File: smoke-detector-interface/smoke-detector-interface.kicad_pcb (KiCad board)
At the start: 2 copper layers, 55.9 x 106.7 mm, 28 parts, among them J1 Conn_01x04_Pin, J2 M50-3500542, J3 DE9_Receptacle, J4 61200621621, J5 Conn_01x06_Pin, U1 UA78L10ACLPRE3, U2 AS7805AT, U3 ATtiny13A-P

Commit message: WIP
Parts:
- JP1: footprint TestPoint:TestPoint_Bridge_Pitch2.54mm_Drill0.7mm -> Resistor_THT:R_Axial_DIN0204_L3.6mm_D1.6mm_P7.62mm_Horizontal
- moved JP1 16.2 mm to (149.9, 127.6), turned to -90 degrees
- moved R3 10.8 mm to (121.3, 112.4)
- moved C4 9.71 mm to (135.8, 109.9)
- moved C9 7.54 mm to (143.5, 137.2), turned to 180 degrees
- moved C3 5.85 mm to (125.8, 109.9)
- moved C2 1.33 mm to (143.2, 142.2)
- moved C1 0.90 mm to (148.0, 118.8)
- moved U3 0.90 mm to (136.5, 118.8)
- moved D2 0.64 mm to (129.5, 116.2)
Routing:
- net +5V: track 43.3 -> 129.7 mm
- net +12V: track 71.3 -> 107.1 mm
- net HOSTTX: track 44.0 -> 70.7 mm
- net HOSTRX: track 94.7 -> 73.0 mm
- net Net-(J5-Pin_4): track 0.00 -> 17.3 mm
- net Net-(J2-Pad9): track 33.2 -> 23.3 mm
- net Net-(U3-PB2): track 10.9 -> 15.1 mm
- net Net-(D2-K): track 11.4 -> 15.3 mm
- net Net-(U3-PB1): track 18.9 -> 21.4 mm
- net Net-(U3-PB0): track 22.2 -> 20.3 mm
- net +10V: track 18.1 -> 17.0 mm
- added copper zone on B.Cu, net GND
- removed copper zone on B.Cu, net +12V

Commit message: Improved routing.
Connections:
- net Net-(U3-PB0) renamed MOSI
- net Net-(U3-PB1) renamed MISO
- net Net-(U3-PB2) renamed SCK
- J4 pad 5: Net-(U3-~{RESET}/PB5) -> _RESET
- J5 pad 3: HOSTTX -> Net-(J5-Pin_3)
- J5 pad 4: Net-(J5-Pin_4) -> HOSTRX
- JP1 pad 1: HOSTRX -> HOSTTX
- JP1 pad 2: Net-(J5-Pin_4) -> Net-(J5-Pin_3)
- U3 pad 1: Net-(U3-~{RESET}/PB5) -> _RESET
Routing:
- net _RESET: track 0.00 -> 59.6 mm
- net HOSTRX: track 73.0 -> 91.6 mm
- net Net-(J5-Pin_4): track 17.3 -> 0.00 mm
- net Net-(U3-~{RESET}/PB5): track 13.0 -> 0.00 mm
- net +5V: track 129.7 -> 135.8 mm
- net MISO: track 21.4 -> 23.2 mm
- net MOSI: track 20.3 -> 21.9 mm

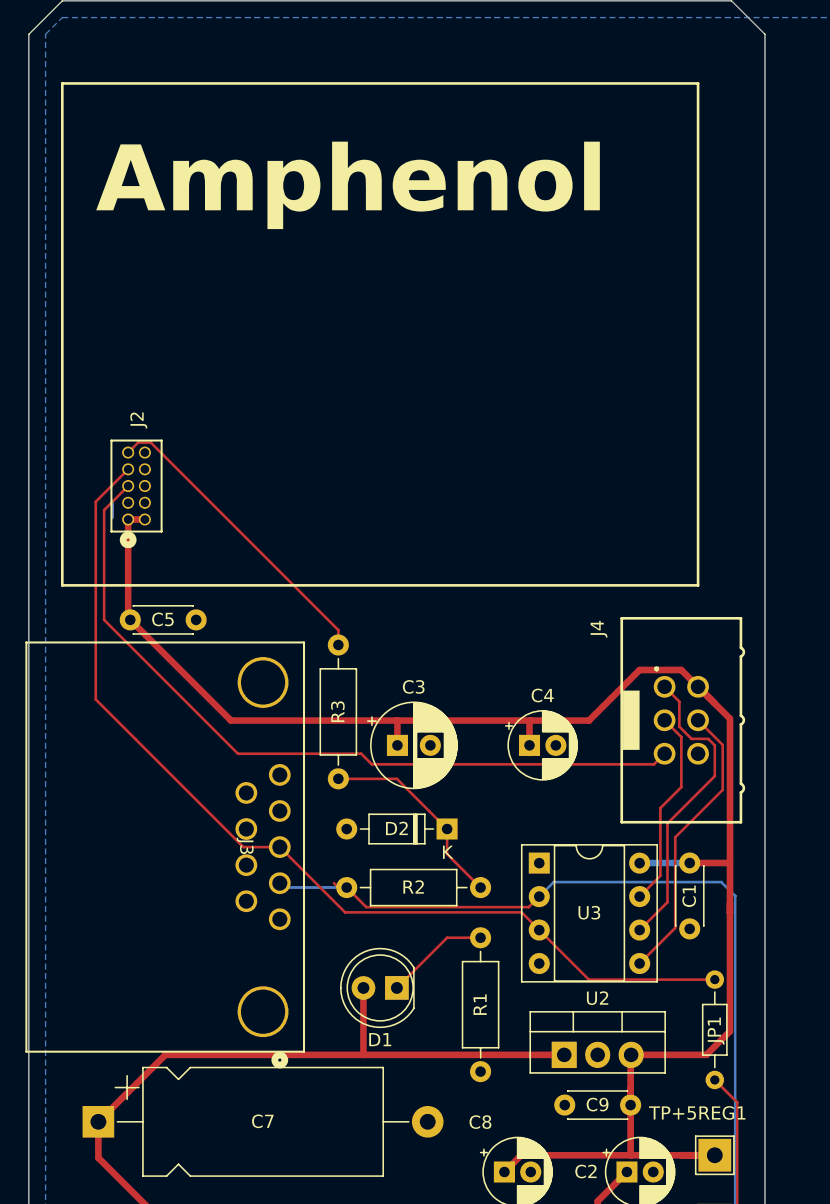
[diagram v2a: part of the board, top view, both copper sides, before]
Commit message: Updates for Zenerglass parts.
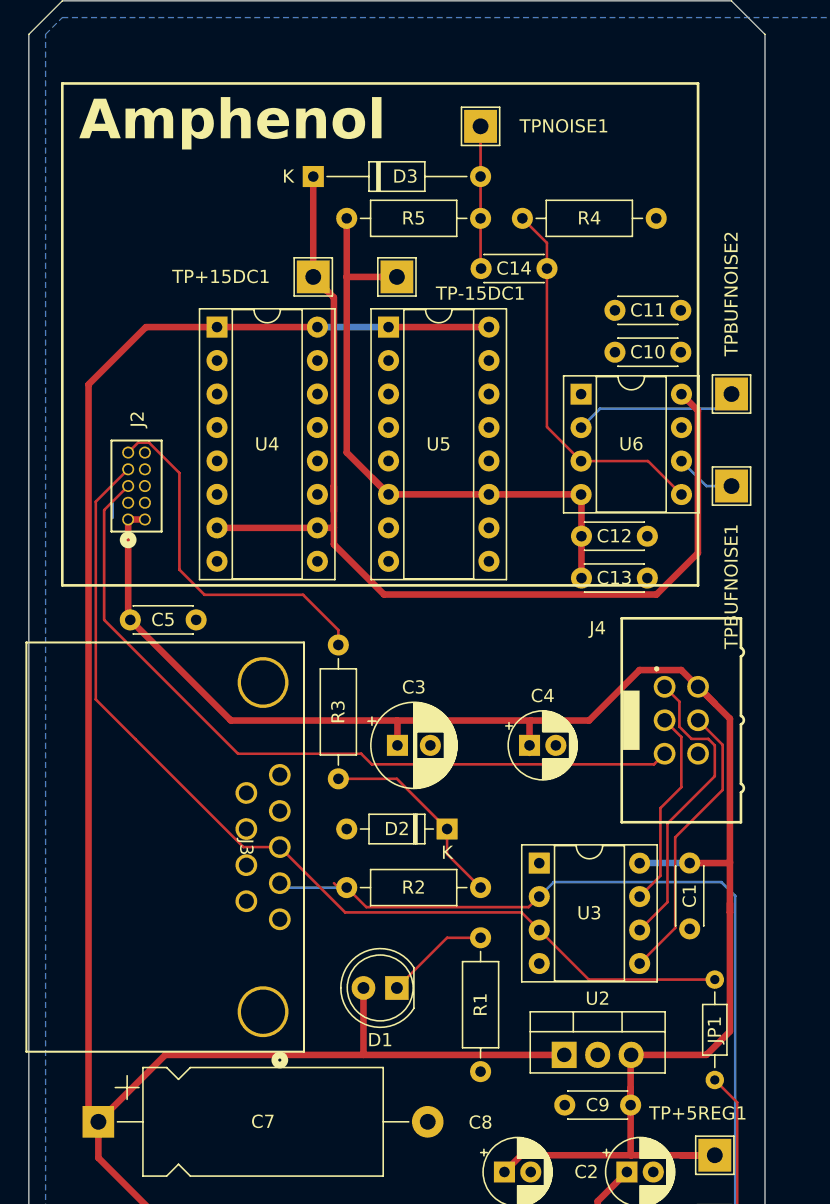
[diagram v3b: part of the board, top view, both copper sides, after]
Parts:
- added C10: 100n, Capacitor_THT:C_Disc_D4.3mm_W1.9mm_P5.00mm, F.Cu at (147.3, 80.0)
- added C11: 1u, Capacitor_THT:C_Disc_D4.3mm_W1.9mm_P5.00mm, F.Cu at (147.3, 76.8)
- added C12: 1u, Capacitor_THT:C_Disc_D4.3mm_W1.9mm_P5.00mm, F.Cu at (139.7, 94.0)
- added C13: 100n, Capacitor_THT:C_Disc_D4.3mm_W1.9mm_P5.00mm, F.Cu at (139.7, 97.2)
- added C14: 1u FILM, Capacitor_THT:C_Disc_D4.3mm_W1.9mm_P5.00mm, F.Cu at (132.1, 73.7)
- added D3: BZX79-C24, Diode_THT:D_DO-35_SOD27_P12.70mm_Horizontal, F.Cu at (119.4, 66.7)
- added R4: 1meg, Resistor_THT:R_Axial_DIN0207_L6.3mm_D2.5mm_P10.16mm_Horizontal, F.Cu at (135.3, 69.8)
- added R5: 100k, Resistor_THT:R_Axial_DIN0207_L6.3mm_D2.5mm_P10.16mm_Horizontal, F.Cu at (132.1, 69.8)
- added TP+15DC1: +15, TestPoint:TestPoint_THTPad_2.5x2.5mm_Drill1.2mm, F.Cu at (119.4, 74.3)
- added TP-15DC1: -15, TestPoint:TestPoint_THTPad_2.5x2.5mm_Drill1.2mm, F.Cu at (125.7, 74.3)
- added TPBUFNOISE1: BUFNOISE, TestPoint:TestPoint_THTPad_2.5x2.5mm_Drill1.2mm, F.Cu at (151.1, 90.2)
- added TPBUFNOISE2: BUFNOISE, TestPoint:TestPoint_THTPad_2.5x2.5mm_Drill1.2mm, F.Cu at (151.1, 83.2)
- added TPNOISE1: NOISE, TestPoint:TestPoint_THTPad_2.5x2.5mm_Drill1.2mm, F.Cu at (132.1, 62.9)
- added U4: ~, Package_DIP:DIP-16_W7.62mm_Socket, F.Cu at (112.1, 78.1)
- added U5: ~, Package_DIP:DIP-16_W7.62mm_Socket, F.Cu at (125.1, 78.1)
- added U6: TL072, Package_DIP:DIP-8_W7.62mm_Socket, F.Cu at (139.7, 83.2)
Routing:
- net +12V: track 107.1 -> 195.6 mm
- net +15V: track 0.00 -> 82.5 mm
- net -15V: track 0.00 -> 48.8 mm
- net Net-(U6A-+): track 0.00 -> 28.9 mm
- net Net-(U6A--): track 0.00 -> 12.5 mm
- net Net-(D3-A): track 0.00 -> 10.8 mm
- net Net-(U6B--): track 0.00 -> 4.58 mm
- net Net-(J2-Pad9): track 23.3 -> 27.6 mm

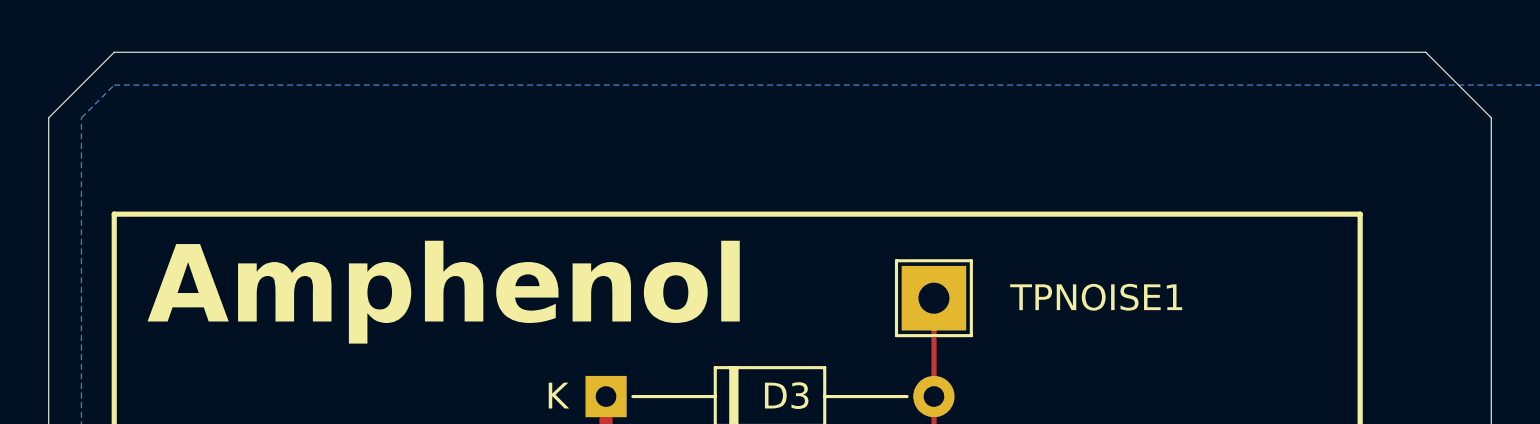
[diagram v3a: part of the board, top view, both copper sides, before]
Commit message: Add mounting holes.
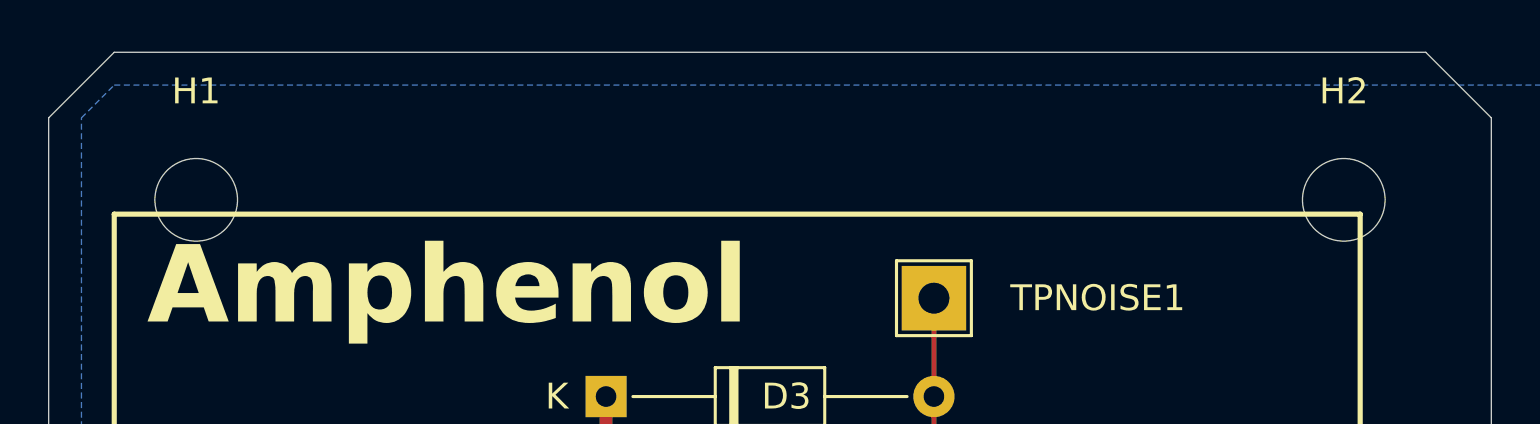
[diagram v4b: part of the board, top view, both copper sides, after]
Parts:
- added H1: MountingHole, MountingHole:MountingHole_3.2mm_M3, F.Cu at (103.5, 59.1)
- added H2: MountingHole, MountingHole:MountingHole_3.2mm_M3, F.Cu at (148.0, 59.1)
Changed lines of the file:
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@@
 		(tags "C Disc series Radial pin pitch 5.00mm  diameter 4.3mm width 1.9mm Capacitor")
 		(property "Reference" "C14"
-			(at 2.5 0 360)
+			(at 2.5 0 0)
 			(layer "F.SilkS")
 			(effects
@@
 		)
 		(property "Value" "1u FILM"
-			(at 2.5 2.2 360)
+			(at 2.5 2.2 0)
 			(layer "F.Fab")
 			(effects
@@
 		)
 		(fp_text user "${REFERENCE}"
-			(at 2.5 0 360)
+			(at 2.5 0 0)
 			(layer "F.Fab")
 			(effects
@@
 		(tags "Resistor Axial_DIN0207 series Axial Horizontal pin pitch 10.16mm 0.25W = 1/4W length 6.3mm diameter 2.5mm")
 		(property "Reference" "R5"
-			(at 5.08 0 360)
+			(at 5.08 0 0)
 			(layer "F.SilkS")
 			(effects
@@
 		)
 		(property "Value" "100k"
-			(at 5.08 2.37 360)
+			(at 5.08 2.37 0)
 			(layer "F.Fab")
 			(effects
@@
 		)
 		(fp_text user "${REFERENCE}"
-			(at 5.08 0 360)
+			(at 5.08 0 0)
 			(layer "F.Fab")
 			(effects
@@
 		)
 	)
+	(footprint "MountingHole:MountingHole_3.2mm_M3"
+		(layer "F.Cu")
+		(at 147.955 59.055)
+		(descr "Mounting Hole 3.2mm, no annular, M3")
+		(tags "mounting hole 3.2mm no annular m3")
+		(property "Reference" "H2"
+			(at 0 -4.2 0)
+			(layer "F.SilkS")
+			(effects
+				(font
+					(size 1 1)
+					(thickness 0.15)
+				)
+			)
+		)
+		(property "Value" "MountingHole"
+			(at 0 4.2 0)
+			(layer "F.Fab")
+			(effects
+				(font
+					(size 1 1)
+					(thickness 0.15)
+				)
+			)
+		)
+		(property "Footprint" "MountingHole:MountingHole_3.2mm_M3"
+			(at 0 0 0)
+			(unlocked yes)
+			(layer "F.Fab")
+			(hide yes)
+			(effects
+				(font
+					(size 1.27 1.27)
+					(thickness 0.15)
+				)
+			)
+		)
+		(property "Datasheet" ""
+			(at 0 0 0)
+			(unlocked yes)
+			(layer "F.Fab")
+			(hide yes)
+			(effects
+				(font
+					(size 1.27 1.27)
+					(thickness 0.15)
+				)
+			)
+		)
+		(property "Description" "Mounting Hole without connection"
+			(at 0 0 0)
+			(unlocked yes)
+			(layer "F.Fab")
+			(hide yes)
+			(effects
+				(font
+					(size 1.27 1.27)
+					(thickness 0.15)
+				)
+			)
+		)
+		(property ki_fp_filters "MountingHole*")
+		(sheetname "Root")
+		(sheetfile "smoke-detector-interface.kicad_sch")
+		(attr exclude_from_pos_files exclude_from_bom)
+		(fp_circle
+			(center 0 0)
+			(end 3.2 0)
+			(stroke
+				(width 0.15)
+				(type solid)
+			)
+			(fill none)
+			(layer "Cmts.User")
+		)
+		(fp_circle
+			(center 0 0)
+			(end 3.45 0)
+			(stroke
+				(width 0.05)
+				(type solid)
+			)
+			(fill none)
+			(layer "F.CrtYd")
+		)
+		(fp_text user "${REFERENCE}"
+			(at 0 0 0)
+			(layer "F.Fab")
+			(effects
+				(font
+					(size 1 1)
+					(thickness 0.15)
+				)
+			)
+		)
+		(pad "" np_thru_hole circle
+			(at 0 0)
+			(size 3.2 3.2)
+			(drill 3.2)
+			(layers "*.Cu" "*.Mask")
+		)
+	)
 	(footprint "Package_TO_SOT_THT:TO-220-3_Vertical"
 		(layer "F.Cu")
@@
 		)
 	)
+	(footprint "MountingHole:MountingHole_3.2mm_M3"
+		(layer "F.Cu")
+		(at 103.505 59.055)
+		(descr "Mounting Hole 3.2mm, no annular, M3")
+		(tags "mounting hole 3.2mm no annular m3")
+		(property "Reference" "H1"
+			(at 0 -4.2 0)
+			(layer "F.SilkS")
+			(effects
+				(font
+					(size 1 1)
+					(thickness 0.15)
+				)
+			)
+		)
+		(property "Value" "MountingHole"
+			(at 0 4.2 0)
+			(layer "F.Fab")
+			(effects
+				(font
+					(size 1 1)
+					(thickness 0.15)
+				)
+			)
+		)
+		(property "Footprint" "MountingHole:MountingHole_3.2mm_M3"
+			(at 0 0 0)
+			(unlocked yes)
+			(layer "F.Fab")
+			(hide yes)
+			(effects
+				(font
+					(size 1.27 1.27)
+					(thickness 0.15)
+				)
+			)
+		)
+		(property "Datasheet" ""
+			(at 0 0 0)
+			(unlocked yes)
+			(layer "F.Fab")
+			(hide yes)
+			(effects
+				(font
+					(size 1.27 1.27)
+					(thickness 0.15)
+				)
+			)
+		)
+		(property "Description" "Mounting Hole without connection"
+			(at 0 0 0)
+			(unlocked yes)
+			(layer "F.Fab")
+			(hide yes)
+			(effects
+				(font
+					(size 1.27 1.27)
+					(thickness 0.15)
+				)
+			)
+		)
+		(property ki_fp_filters "MountingHole*")
+		(sheetname "Root")
+		(sheetfile "smoke-detector-interface.kicad_sch")
+		(attr exclude_from_pos_files exclude_from_bom)
+		(fp_circle
+			(center 0 0)
+			(end 3.2 0)
+			(stroke
+				(width 0.15)
+				(type solid)
+			)
+			(fill none)
+			(layer "Cmts.User")
+		)
+		(fp_circle
+			(center 0 0)
+			(end 3.45 0)
+			(stroke
+				(width 0.05)
+				(type solid)
+			)
+			(fill none)
+			(layer "F.CrtYd")
+		)
+		(fp_text user "${REFERENCE}"
+			(at 0 0 0)
+			(layer "F.Fab")
+			(effects
+				(font
+					(size 1 1)
+					(thickness 0.15)
+				)
+			)
+		)
+		(pad "" np_thru_hole circle
+			(at 0 0)
+			(size 3.2 3.2)
+			(drill 3.2)
+			(layers "*.Cu" "*.Mask")
+		)
+	)
 	(footprint "Capacitor_THT:CP_Radial_D5.0mm_P2.00mm"
 		(layer "F.Cu")
@@
 		(tags "C Disc series Radial pin pitch 5.00mm  diameter 4.3mm width 1.9mm Capacitor")
 		(property "Reference" "C10"
-			(at 2.5 0 360)
+			(at 2.5 0 0)
 			(layer "F.SilkS")
 			(effects
@@
 		)
 		(property "Value" "100n"
-			(at 2.5 2.2 360)
+			(at 2.5 2.2 0)
 			(layer "F.Fab")
 			(effects
@@
 		)
 		(fp_text user "${REFERENCE}"
-			(at 2.5 0 360)
+			(at 2.5 0 0)
 			(layer "F.Fab")
 			(effects
@@
 		(tags "Diode DO-35_SOD27 series Axial Horizontal pin pitch 12.7mm  length 4mm diameter 2mm")
 		(property "Reference" "D3"
-			(at 6.985 0 360)
+			(at 6.985 0 0)
 			(layer "F.SilkS")
 			(effects
@@
 		)
 		(property "Value" "BZX79-C24"
-			(at 6.35 2.12 360)
+			(at 6.35 2.12 0)
 			(layer "F.Fab")
 			(effects
@@
 		)
 		(fp_text user "K"
-			(at -1.905 0 360)
+			(at -1.905 0 0)
 			(layer "F.SilkS")
 			(effects
@@
 		)
 		(fp_text user "K"
-			(at 0 -1.8 360)
+			(at 0 -1.8 0)
 			(layer "F.Fab")
 			(effects
@@
 		)
 		(fp_text user "${REFERENCE}"
-			(at 6.65 0 360)
+			(at 6.65 0 0)
 			(layer "F.Fab")
 			(effects
@@
 		(tags "C Disc series Radial pin pitch 5.00mm  diameter 4.3mm width 1.9mm Capacitor")
 		(property "Reference" "C11"
-			(at 2.5 0 360)
+			(at 2.5 0 0)
 			(layer "F.SilkS")
 			(effects
@@
 		)
 		(property "Value" "1u"
-			(at 2.5 2.2 360)
+			(at 2.5 2.2 0)
 			(layer "F.Fab")
 			(effects
@@
 		)
 		(fp_text user "${REFERENCE}"
-			(at 2.5 0 360)
+			(at 2.5 0 0)
 			(layer "F.Fab")
 			(effects

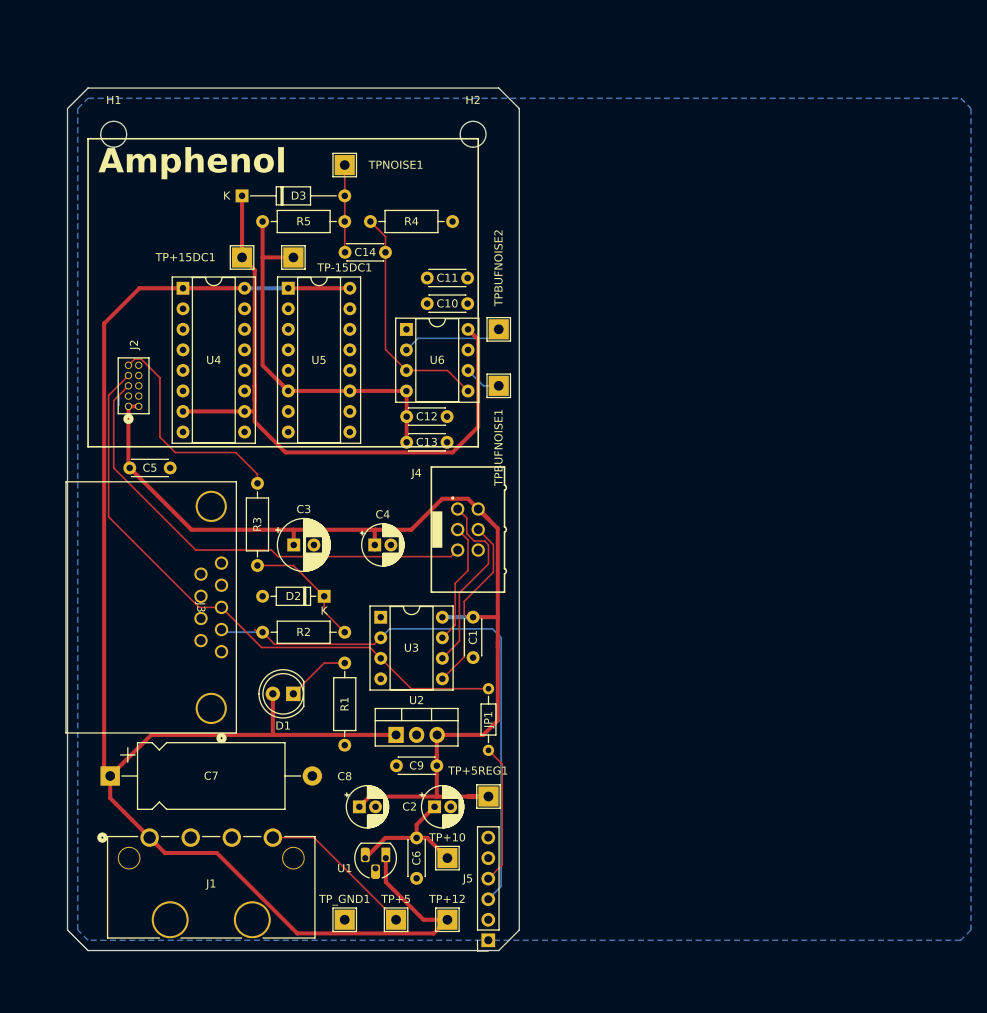
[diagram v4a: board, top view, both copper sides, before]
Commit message: DRC passes.
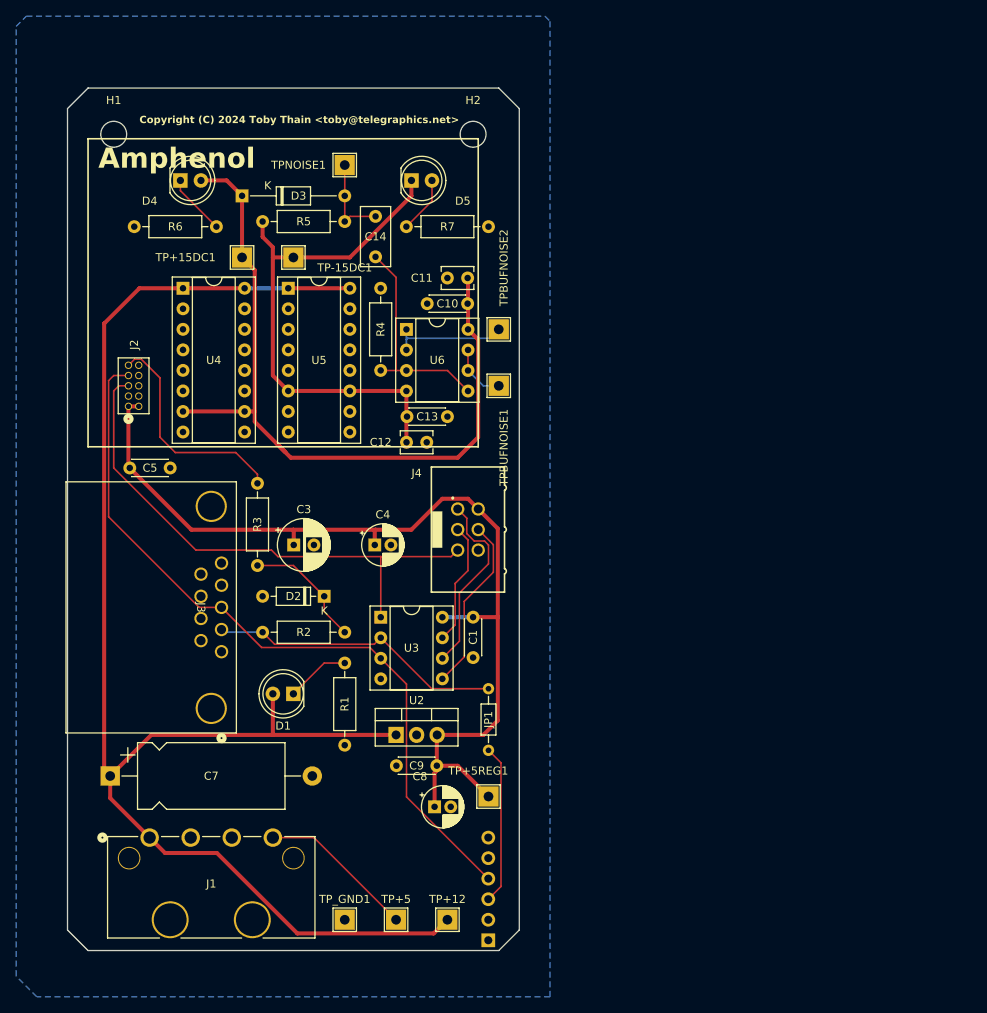
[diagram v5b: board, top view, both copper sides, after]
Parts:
- removed C2: 22u, Capacitor_THT:CP_Radial_D5.0mm_P2.00mm
- removed C6: 100n, Capacitor_THT:C_Disc_D4.3mm_W1.9mm_P5.00mm
- removed TP+10: +10, TestPoint:TestPoint_THTPad_2.5x2.5mm_Drill1.2mm
- removed U1: UA78L10ACLPRE3, Package_TO_SOT_THT:TO-92_HandSolder
- added D4: LED, LED_THT:LED_D5.0mm, F.Cu at (111.8, 64.8)
- added D5: LED, LED_THT:LED_D5.0mm, F.Cu at (140.3, 64.8)
- added R6: 1k, Resistor_THT:R_Axial_DIN0207_L6.3mm_D2.5mm_P10.16mm_Horizontal, F.Cu at (116.2, 70.5)
- added R7: 1k, Resistor_THT:R_Axial_DIN0207_L6.3mm_D2.5mm_P10.16mm_Horizontal, F.Cu at (149.9, 70.5)
- C11, C12: footprint Capacitor_THT:C_Disc_D4.3mm_W1.9mm_P5.00mm -> Capacitor_THT:C_Disc_D3.8mm_W2.6mm_P2.50mm
- C14: value 1u FILM -> .47u FILM; footprint Capacitor_THT:C_Disc_D4.3mm_W1.9mm_P5.00mm -> Capacitor_THT:C_Rect_L7.2mm_W3.5mm_P5.00mm_FKS2_FKP2_MKS2_MKP2
- J5: footprint Connector_PinSocket_2.54mm:PinSocket_1x06_P2.54mm_Vertical -> Connector_PinHeader_2.54mm:PinHeader_1x06_P2.54mm_Vertical; moved to B.Cu
- moved R4 18.5 mm to (136.5, 88.3), turned to 90 degrees
- moved C8 9.30 mm to (143.2, 142.2)
- moved C14 5.83 mm to (135.9, 69.2), turned to -90 degrees
- moved C13 3.18 mm to (139.8, 94.0)
- moved C12 3.18 mm to (139.7, 97.2)
- turned J5 to 0 degrees
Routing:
- net HOSTTX: track 70.7 -> 36.7 mm
- net Net-(J5-Pin_3): track 0.00 -> 19.7 mm
- net +10V: track 17.0 -> 0.00 mm
- net -15V: track 48.8 -> 65.4 mm
- net +5V: track 135.8 -> 120.4 mm
- net +15V: track 82.5 -> 95.6 mm
- net +12V: track 195.6 -> 183.1 mm
- net Net-(D4-K): track 0.00 -> 7.56 mm
- net Net-(D5-A): track 0.00 -> 7.03 mm
- net _RESET: track 59.6 -> 66.5 mm
- net Net-(U6B--): track 4.58 -> 7.12 mm
- net Net-(U6A--): track 12.5 -> 14.5 mm
- net Net-(U6A-+): track 28.9 -> 27.0 mm
- net HOSTRX: track 91.6 -> 93.2 mm
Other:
- board text added: "Copyright (C) 2024 Toby Thain <toby@telegraphics.net>"
